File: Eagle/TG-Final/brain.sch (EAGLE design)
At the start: 5 parts

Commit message: Peliando con un 16f88
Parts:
- removed U$5: UK1122, aasanchez:UK1122
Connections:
- new net N$1: U$1.PIN15
- new net N$2: U$1.PIN14
- new net N$3: U$1.PIN13
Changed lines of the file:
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@@
 <part name="+3V1" library="supply1" deviceset="+3V3" device=""/>
 <part name="U$6" library="adafruit" deviceset="ARDUINO" device="-NOHOLE"/>
-<part name="U$5" library="aasanchez" deviceset="UK1122" device=""/>
 <part name="U$7" library="aasanchez" deviceset="IMU3000COMBO" device=""/>
 <part name="+3V2" library="supply1" deviceset="+3V3" device=""/>
@@
 </segment>
 </net>
+<net name="N$1" class="0">
+<segment>
+<pinref part="U$1" gate="G$1" pin="PIN15"/>
+<wire x1="-5.08" y1="2.54" x2="-10.16" y2="2.54" width="0.1524" layer="91"/>
+</segment>
+</net>
+<net name="N$2" class="0">
+<segment>
+<pinref part="U$1" gate="G$1" pin="PIN14"/>
+<wire x1="-5.08" y1="5.08" x2="-10.16" y2="5.08" width="0.1524" layer="91"/>
+</segment>
+</net>
+<net name="N$3" class="0">
+<segment>
+<pinref part="U$1" gate="G$1" pin="PIN13"/>
+<wire x1="-5.08" y1="7.62" x2="-10.16" y2="7.62" width="0.1524" layer="91"/>
+</segment>
+</net>
 </nets>
 </sheet>
@@
 </instances>
 <busses>
-</busses>
-<nets>
-</nets>
-</sheet>
-<sheet>
-<plain>
-</plain>
-<instances>
-<instance part="U$5" gate="G$1" x="0" y="0"/>
-</instances>
-<busses>

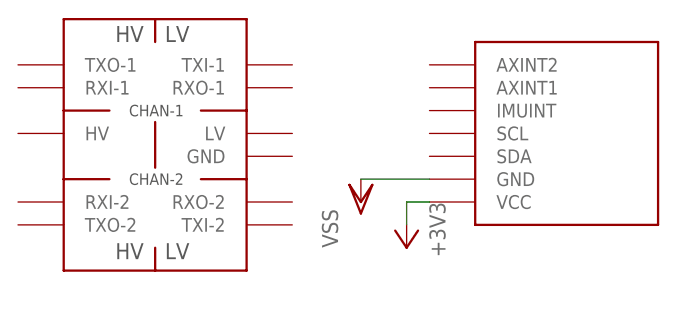
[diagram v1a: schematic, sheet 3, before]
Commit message: Placa de Control Motores y Comunicación
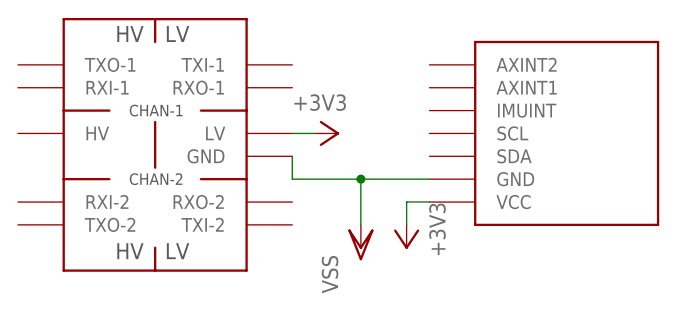
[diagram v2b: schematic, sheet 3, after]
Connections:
- net +3V3: now also U$8.LV
- net VSS: now also U$8.GND
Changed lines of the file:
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@@
 <part name="VSS2" library="supply1" deviceset="VSS" device=""/>
 <part name="U$8" library="aasanchez" deviceset="LOGIC-LEVEL-CONVERTER" device=""/>
+<part name="+3V3" library="supply1" deviceset="+3V3" device=""/>
 </parts>
 <sheets>
@@
 <instance part="U$7" gate="G$1" x="0" y="0"/>
 <instance part="+3V2" gate="G$1" x="-7.62" y="-2.54" rot="R180"/>
-<instance part="VSS2" gate="G$1" x="-12.7" y="2.54"/>
+<instance part="VSS2" gate="G$1" x="-12.7" y="-2.54"/>
 <instance part="U$8" gate="G$1" x="-25.4" y="-5.08" rot="MR0"/>
+<instance part="+3V3" gate="G$1" x="-15.24" y="10.16" rot="R270"/>
 </instances>
 <busses>
@@
 <net name="+3V3" class="0">
 <segment>
+<pinref part="+3V2" gate="G$1" pin="+3V3"/>
+<wire x1="-7.62" y1="2.54" x2="-7.62" y2="0" width="0.1524" layer="91"/>
 <pinref part="U$7" gate="G$1" pin="VCC"/>
-<pinref part="+3V2" gate="G$1" pin="+3V3"/>
 <wire x1="-5.08" y1="2.54" x2="-7.62" y2="2.54" width="0.1524" layer="91"/>
-<wire x1="-7.62" y1="2.54" x2="-7.62" y2="0" width="0.1524" layer="91"/>
+</segment>
+<segment>
+<pinref part="+3V3" gate="G$1" pin="+3V3"/>
+<pinref part="U$8" gate="G$1" pin="LV"/>
+<wire x1="-17.78" y1="10.16" x2="-20.32" y2="10.16" width="0.1524" layer="91"/>
 </segment>
 </net>
@@
 <pinref part="VSS2" gate="G$1" pin="VSS"/>
 <wire x1="-5.08" y1="5.08" x2="-12.7" y2="5.08" width="0.1524" layer="91"/>
+<wire x1="-12.7" y1="5.08" x2="-12.7" y2="0" width="0.1524" layer="91"/>
+<pinref part="U$8" gate="G$1" pin="GND"/>
+<wire x1="-20.32" y1="5.08" x2="-20.32" y2="7.62" width="0.1524" layer="91"/>
+<wire x1="-20.32" y1="5.08" x2="-12.7" y2="5.08" width="0.1524" layer="91"/>
+<junction x="-12.7" y="5.08"/>
 </segment>
 </net>

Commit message: Listo Placas
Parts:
- U$6: value ARDUINO-NOHOLE -> ARDUINOUNO; device adafruit:ARDUINO-NOHOLE -> adafruit:ARDUINOUNO
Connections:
- removed net +11V1: U$1.PIN19
- removed net +12V: U$1.PIN18
- removed net +22V: U$1.PIN17
- removed net +6V: U$1.PIN20
- removed net N$3: U$1.PIN13
- new net M1-A: U$1.PIN05, U$6.D13
- new net M1-B: U$1.PIN03, U$6.D12
- new net M2-A: U$1.PIN02, U$6.D8
- new net M2-B: U$1.PIN00, U$6.D7
- new net PWM1: U$1.PIN04, U$6.PWM-D11
- new net PWM2: U$1.PIN01, U$6.PWM-D9
- new net RX: U$1.PIN06, U$6.RX-D0
- new net SCL: U$6.A5-SCL, U$8.TXO-1
- new net SDA: U$6.A4-SDA, U$8.TXO-2
- new net SERVO1: U$1.PIN24, U$6.PWM-D10
- new net SERVO2: U$1.PIN27, U$6.PWM-D3
- new net SERVO3: U$1.PIN26, U$6.PWM-D5
- new net SERVO4: U$1.PIN25, U$6.PWM-D6
- new net TX: U$1.PIN07, U$6.TX-D1
- net +3V3: now also U$1.+3V3; no longer U$1.PIN22
- net N$1: now also U$7.SCL, U$8.TXI-1; no longer U$1.PIN15
- net N$2: now also U$7.SDA, U$8.TXI-2; no longer U$1.PIN14
- net VDD: now also U$1.+5V, U$6.5V, U$8.HV; no longer U$1.PIN21
- net VSS: now also U$1.VSS, U$6.GND1, U$6.GND2, U$8.@GND; no longer U$1.PIN16

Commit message: Actualizaciones Varias
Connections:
- new net N$5: U$6.3V
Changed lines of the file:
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@@
+</segment>
+</net>
+<net name="N$5" class="0">
+<segment>
+<pinref part="U$6" gate="G$1" pin="3V"/>
+<wire x1="-5.08" y1="27.94" x2="-10.16" y2="27.94" width="0.1524" layer="91"/>
 </segment>
 </net>
